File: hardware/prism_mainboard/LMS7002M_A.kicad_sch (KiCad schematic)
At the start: 1 part, among them U2 LMS7002M

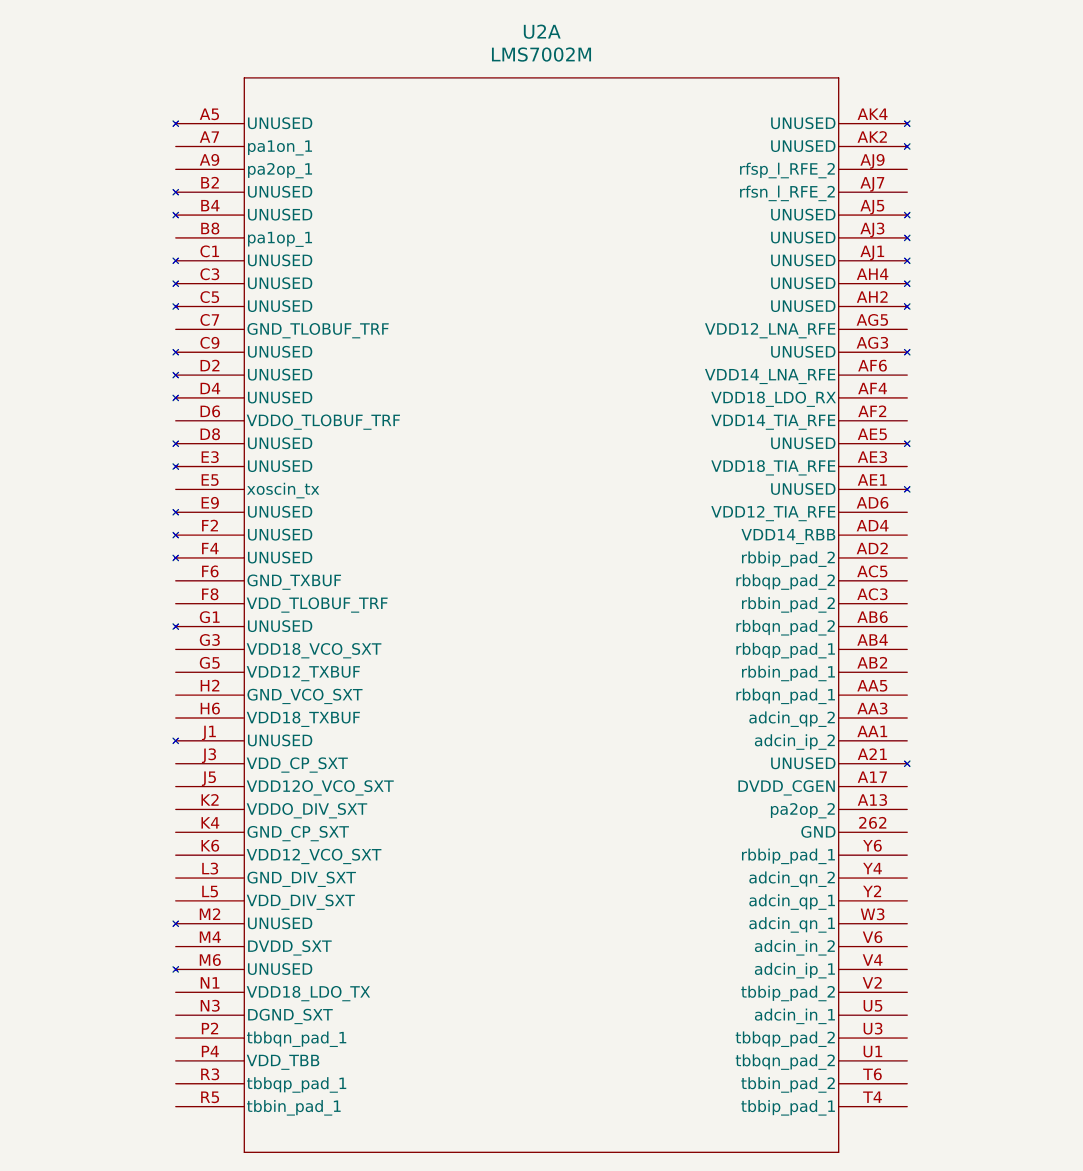
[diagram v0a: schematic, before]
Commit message: Mainboard Updates
Started a lot of the basic schematic nets like GND and Power nets. Major Change: Decided on using the XC7Z015-1CLG485I instead of the 7010 or 7020 due to the ability to use HDMI interfaces with an adapter and more LUTs. Updated schematic symbols and footprints accordingly. Added Memory, Encoder, MicroSD schematics. Added LimeSDR footprints as well. Will Try to add Power to the entire board next.
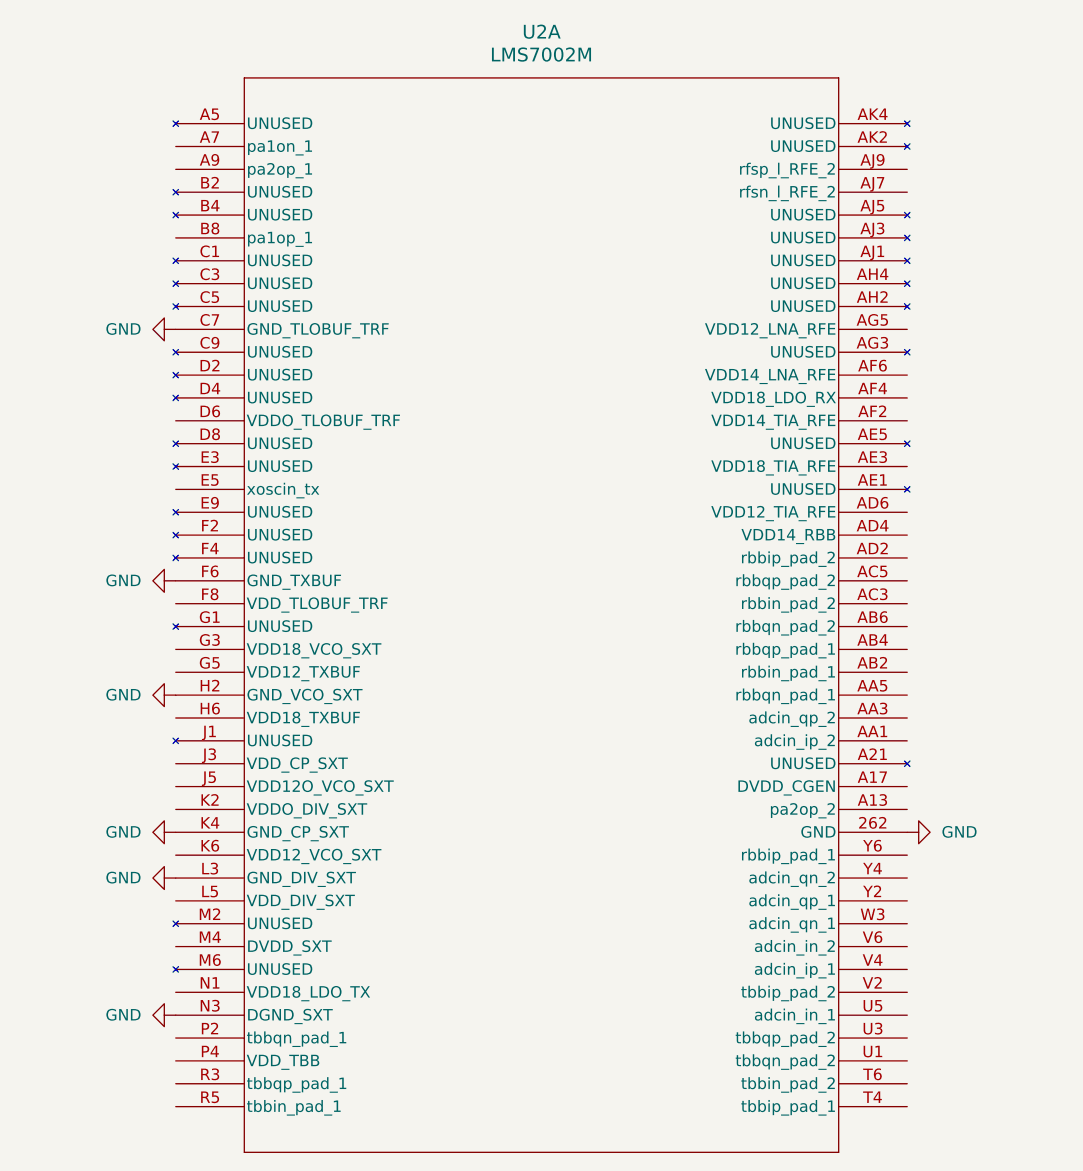
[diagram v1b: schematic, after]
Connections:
- net GND: now reaches U2.262 (GND)
- net GND: now also U2.C7 (GND_TLOBUF_TRF), U2.F6 (GND_TXBUF), U2.H2 (GND_VCO_SXT), U2.K4 (GND_CP_SXT), U2.L3 (GND_DIV_SXT), U2.N3 (DGND_SXT)

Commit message: Schematic Updates
Updated schematics. Most of the power and decoupling is set for most if not all devices. Need to interconnect devices. Still reading datasheets
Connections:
- net VDD_1V8: now reaches U2.AE3 (VDD18_TIA_RFE)
- net VDD_1V8: now also U2.G3 (VDD18_VCO_SXT)
- net VDD_1V8_LDO: now reaches U2.AF4 (VDD18_LDO_RX)
- net VDD_1V8_LDO: now also U2.N1 (VDD18_LDO_TX)
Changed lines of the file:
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@@
 	(generator_version "10.0")
 	(paper "A4")
+	(global_label "VDD_1V8"
+		(shape input)
+		(at 176.53 73.66 0)
+		(fields_autoplaced yes)
+		(effects
+			(font
+				(size 1.27 1.27)
+			)
+			(justify left)
+		)
+		(property "Intersheetrefs" "${INTERSHEET_REFS}"
+			(at 187.619 73.66 0)
+			(hide yes)
+			(show_name no)
+			(do_not_autoplace no)
+			(effects
+				(font
+					(size 1.27 1.27)
+				)
+				(justify left)
+			)
+		)
+	)
+	(global_label "VDD_1V8_LDO"
+		(shape input)
+		(at 95.25 132.08 180)
+		(fields_autoplaced yes)
+		(effects
+			(font
+				(size 1.27 1.27)
+			)
+			(justify right)
+		)
+		(property "Intersheetrefs" "${INTERSHEET_REFS}"
+			(at 79.5648 132.08 0)
+			(hide yes)
+			(show_name no)
+			(do_not_autoplace no)
+			(effects
+				(font
+					(size 1.27 1.27)
+				)
+				(justify right)
+			)
+		)
+	)
+	(global_label "VDD_1V8"
+		(shape input)
+		(at 95.25 93.98 180)
+		(fields_autoplaced yes)
+		(effects
+			(font
+				(size 1.27 1.27)
+			)
+			(justify right)
+		)
+		(property "Intersheetrefs" "${INTERSHEET_REFS}"
+			(at 84.161 93.98 0)
+			(hide yes)
+			(show_name no)
+			(do_not_autoplace no)
+			(effects
+				(font
+					(size 1.27 1.27)
+				)
+				(justify right)
+			)
+		)
+	)
+	(global_label "VDD_1V8_LDO"
+		(shape input)
+		(at 176.53 66.04 0)
+		(fields_autoplaced yes)
+		(effects
+			(font
+				(size 1.27 1.27)
+			)
+			(justify left)
+		)
+		(property "Intersheetrefs" "${INTERSHEET_REFS}"
+			(at 192.2152 66.04 0)
+			(hide yes)
+			(show_name no)
+			(do_not_autoplace no)
+			(effects
+				(font
+					(size 1.27 1.27)
+				)
+				(justify left)
+			)
+		)
+	)
 	(symbol
 		(lib_id "power:GND")
